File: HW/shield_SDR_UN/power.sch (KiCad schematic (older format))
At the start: 16 parts

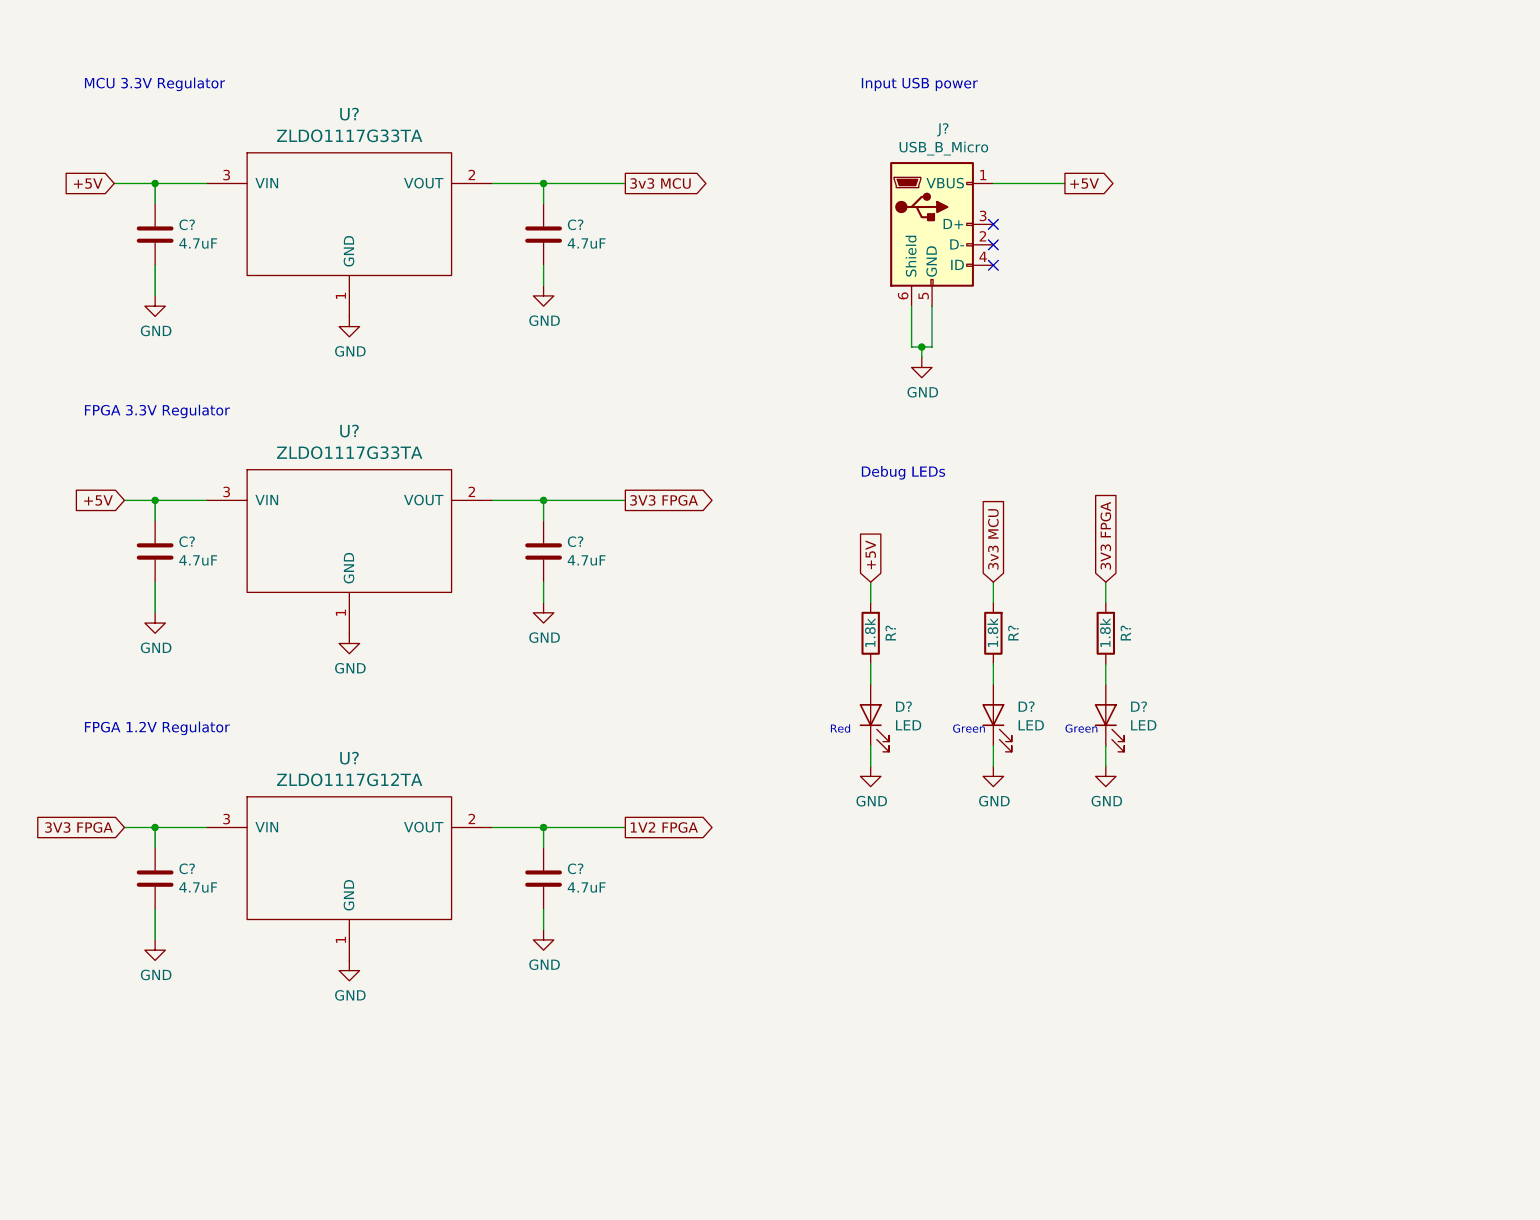
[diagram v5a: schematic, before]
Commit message: algunos footprint
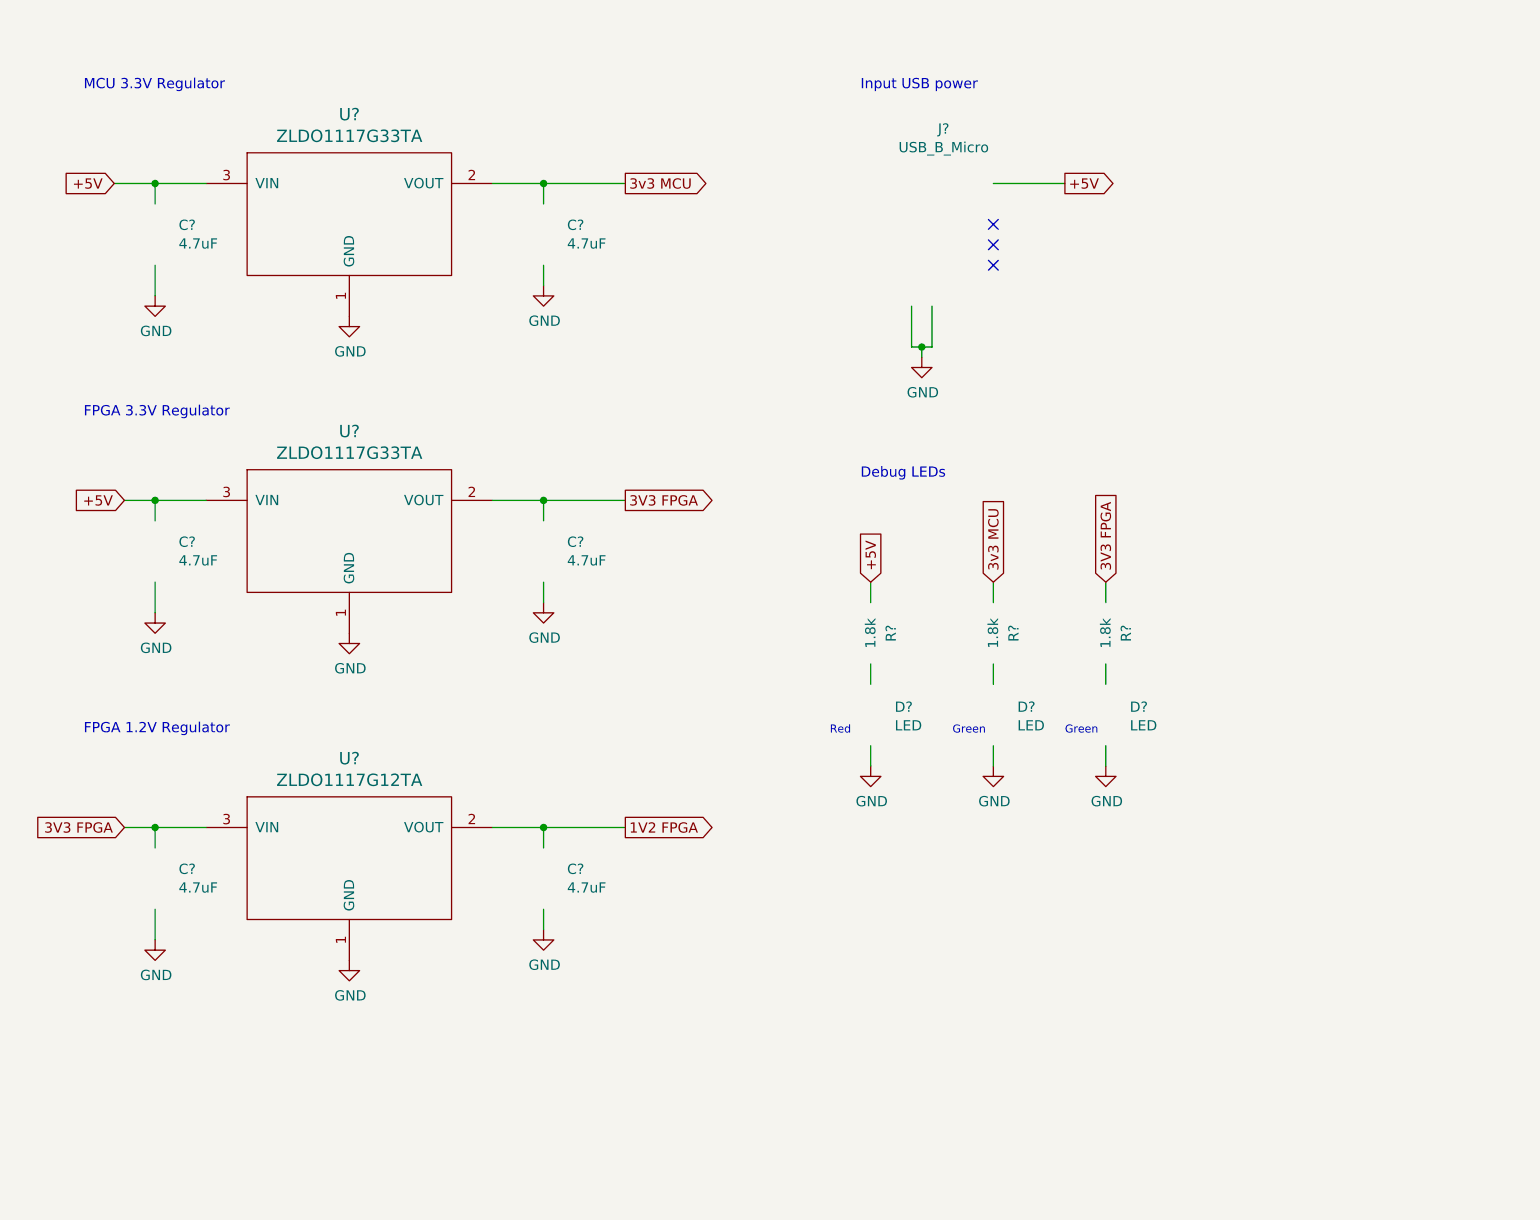
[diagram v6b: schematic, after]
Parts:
- C? (x6): footprint (none) -> Capacitor_SMD:C_0603_1608Metric_Pad1.05x0.95mm_HandSolder
- D? (x3): footprint (none) -> LED_SMD:LED_0805_2012Metric_Pad1.15x1.40mm_HandSolder
- J?: footprint (none) -> Connector_USB:USB_Micro-B_GCT_USB3076-30-A
- R? (x3): footprint (none) -> Resistor_SMD:R_0603_1608Metric_Pad1.05x0.95mm_HandSolder
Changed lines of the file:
@@
 $Comp
 L Device:C C?
-U 1 1 5CCD952E
+U 0 0 5CCD952E
 P 1550 3550
 F 0 "C?" H 1665 3596 50  0000 L CNN
 F 1 "4.7uF" H 1665 3505 50  0000 L CNN
-F 2 "" H 1588 3400 50  0001 C CNN
+F 2 "Capacitor_SMD:C_0603_1608Metric_Pad1.05x0.95mm_HandSolder" H 1588 3400 50  0001 C CNN
 F 3 "~" H 1550 3550 50  0001 C CNN
-	1    1550 3550
-	1    0    0    -1
-$EndComp
-$Comp
-L Device:C C?
-U 1 1 5CCDBE29
+	0    1550 3550
+	1    0    0    -1
+$EndComp
+$Comp
+L Device:C C?
+U 0 0 5CCDBE29
 P 3450 3550
 F 0 "C?" H 3565 3596 50  0000 L CNN
 F 1 "4.7uF" H 3565 3505 50  0000 L CNN
-F 2 "" H 3488 3400 50  0001 C CNN
+F 2 "Capacitor_SMD:C_0603_1608Metric_Pad1.05x0.95mm_HandSolder" H 3488 3400 50  0001 C CNN
 F 3 "~" H 3450 3550 50  0001 C CNN
-	1    3450 3550
+	0    3450 3550
 	1    0    0    -1
 $EndComp
@@
 	3450 3400 3450 3300
 $Comp
-L power:GND #PWR?
+L power:GND #PWR0180
 U 1 1 5CCE00C1
 P 3450 3800
-F 0 "#PWR?" H 3450 3550 50  0001 C CNN
+F 0 "#PWR0180" H 3450 3550 50  0001 C CNN
 F 1 "GND" H 3455 3627 50  0000 C CNN
 F 2 "" H 3450 3800 50  0001 C CNN
@@
 	3450 3700 3450 3800
 $Comp
-L power:GND #PWR?
+L power:GND #PWR0181
 U 1 1 5CCE4197
 P 1550 3850
-F 0 "#PWR?" H 1550 3600 50  0001 C CNN
+F 0 "#PWR0181" H 1550 3600 50  0001 C CNN
 F 1 "GND" H 1555 3677 50  0000 C CNN
 F 2 "" H 1550 3850 50  0001 C CNN
@@
 $Comp
 L Device:C C?
-U 1 1 5CCEBA00
+U 0 0 5CCEBA00
 P 1550 5150
 F 0 "C?" H 1665 5196 50  0000 L CNN
 F 1 "4.7uF" H 1665 5105 50  0000 L CNN
-F 2 "" H 1588 5000 50  0001 C CNN
+F 2 "Capacitor_SMD:C_0603_1608Metric_Pad1.05x0.95mm_HandSolder" H 1588 5000 50  0001 C CNN
 F 3 "~" H 1550 5150 50  0001 C CNN
-	1    1550 5150
+	0    1550 5150
 	1    0    0    -1
 $EndComp
@@
 	3450 5000 3450 4900
 $Comp
-L power:GND #PWR?
+L power:GND #PWR0182
 U 1 1 5CCEBA22
 P 3450 5400
-F 0 "#PWR?" H 3450 5150 50  0001 C CNN
+F 0 "#PWR0182" H 3450 5150 50  0001 C CNN
 F 1 "GND" H 3455 5227 50  0000 C CNN
 F 2 "" H 3450 5400 50  0001 C CNN
@@
 	1550 4900 1550 5000
 $Comp
-L power:GND #PWR?
+L power:GND #PWR0183
 U 1 1 5CCEBA40
 P 1550 5450
-F 0 "#PWR?" H 1550 5200 50  0001 C CNN
+F 0 "#PWR0183" H 1550 5200 50  0001 C CNN
 F 1 "GND" H 1555 5277 50  0000 C CNN
 F 2 "" H 1550 5450 50  0001 C CNN
@@
 $Comp
 L Device:C C?
-U 1 1 5CD3AA6A
+U 0 0 5CD3AA6A
 P 1550 2000
 F 0 "C?" H 1665 2046 50  0000 L CNN
 F 1 "4.7uF" H 1665 1955 50  0000 L CNN
-F 2 "" H 1588 1850 50  0001 C CNN
+F 2 "Capacitor_SMD:C_0603_1608Metric_Pad1.05x0.95mm_HandSolder" H 1588 1850 50  0001 C CNN
 F 3 "~" H 1550 2000 50  0001 C CNN
-	1    1550 2000
-	1    0    0    -1
-$EndComp
-$Comp
-L Device:C C?
-U 1 1 5CD3AA74
+	0    1550 2000
+	1    0    0    -1
+$EndComp
+$Comp
+L Device:C C?
+U 0 0 5CD3AA74
 P 3450 2000
 F 0 "C?" H 3565 2046 50  0000 L CNN
 F 1 "4.7uF" H 3565 1955 50  0000 L CNN
-F 2 "" H 3488 1850 50  0001 C CNN
+F 2 "Capacitor_SMD:C_0603_1608Metric_Pad1.05x0.95mm_HandSolder" H 3488 1850 50  0001 C CNN
 F 3 "~" H 3450 2000 50  0001 C CNN
-	1    3450 2000
+	0    3450 2000
 	1    0    0    -1
 $EndComp
@@
 	3450 1850 3450 1750
 $Comp
-L power:GND #PWR?
+L power:GND #PWR0184
 U 1 1 5CD3AA8C
 P 3450 2250
-F 0 "#PWR?" H 3450 2000 50  0001 C CNN
+F 0 "#PWR0184" H 3450 2000 50  0001 C CNN
 F 1 "GND" H 3455 2077 50  0000 C CNN
 F 2 "" H 3450 2250 50  0001 C CNN
@@
 	3450 2150 3450 2250
 $Comp
-L power:GND #PWR?
+L power:GND #PWR0185
 U 1 1 5CD3AAAA
 P 1550 2300
-F 0 "#PWR?" H 1550 2050 50  0001 C CNN
+F 0 "#PWR0185" H 1550 2050 50  0001 C CNN
 F 1 "GND" H 1555 2127 50  0000 C CNN
 F 2 "" H 1550 2300 50  0001 C CNN
@@
 $Comp
 L Connector:USB_B_Micro J?
-U 1 1 5D009192
+U 0 0 5D009192
 P 5350 1950
 F 0 "J?" H 5407 2417 50  0000 C CNN
 F 1 "USB_B_Micro" H 5407 2326 50  0000 C CNN
-F 2 "" H 5500 1900 50  0001 C CNN
+F 2 "Connector_USB:USB_Micro-B_GCT_USB3076-30-A" H 5500 1900 50  0001 C CNN
 F 3 "~" H 5500 1900 50  0001 C CNN
-	1    5350 1950
+	0    5350 1950
 	1    0    0    -1
 $EndComp
@@
 	5350 2550 5350 2350
 $Comp
-L power:GND #PWR?
+L power:GND #PWR0186
 U 1 1 5D010F02
 P 5300 2600
-F 0 "#PWR?" H 5300 2350 50  0001 C CNN
+F 0 "#PWR0186" H 5300 2350 50  0001 C CNN
 F 1 "GND" H 5305 2427 50  0000 C CNN
 F 2 "" H 5300 2600 50  0001 C CNN
@@
 $Comp
 L Device:C C?
-U 1 1 5CCEBA0A
+U 0 0 5CCEBA0A
 P 3450 5150
 F 0 "C?" H 3565 5196 50  0000 L CNN
 F 1 "4.7uF" H 3565 5105 50  0000 L CNN
-F 2 "" H 3488 5000 50  0001 C CNN
+F 2 "Capacitor_SMD:C_0603_1608Metric_Pad1.05x0.95mm_HandSolder" H 3488 5000 50  0001 C CNN
 F 3 "~" H 3450 5150 50  0001 C CNN
-	1    3450 5150
-	1    0    0    -1
-$EndComp
-$Comp
-L power:GND #PWR?
+	0    3450 5150
+	1    0    0    -1
+$EndComp
+$Comp
+L power:GND #PWR0187
 U 1 1 5CDC3540
 P 2500 3950
-F 0 "#PWR?" H 2500 3700 50  0001 C CNN
+F 0 "#PWR0187" H 2500 3700 50  0001 C CNN
 F 1 "GND" H 2505 3777 50  0000 C CNN
 F 2 "" H 2500 3950 50  0001 C CNN
@@
 $EndComp
 $Comp
-L power:GND #PWR?
+L power:GND #PWR0188
 U 1 1 5CDC3B98
 P 2500 2400
-F 0 "#PWR?" H 2500 2150 50  0001 C CNN
+F 0 "#PWR0188" H 2500 2150 50  0001 C CNN
 F 1 "GND" H 2505 2227 50  0000 C CNN
 F 2 "" H 2500 2400 50  0001 C CNN
@@
 $Comp
 L Device:R R?
-U 1 1 5CE70567
+U 0 0 5CE70567
 P 5050 3950
 AR Path="/5CC081D2/5CE70567" Ref="R?"  Part="1"
-AR Path="/5CC08321/5CE70567" Ref="R?"  Part="1"
+AR Path="/5CC08321/5CE70567" Ref="R?"  Part="0"
 F 0 "R?" V 4950 3950 50  0000 C CNN
 F 1 "1.8k" V 5050 3950 50  0000 C CNN
-F 2 "" V 4980 3950 50  0001 C CNN
+F 2 "Resistor_SMD:R_0603_1608Metric_Pad1.05x0.95mm_HandSolder" V 4980 3950 50  0001 C CNN
 F 3 "~" H 5050 3950 50  0001 C CNN
-	1    5050 3950
+	0    5050 3950
 	-1   0    0    1
 $EndComp
 $Comp
 L Device:LED D?
-U 1 1 5CE70571
+U 0 0 5CE70571
 P 5050 4350
 AR Path="/5CC081D2/5CE70571" Ref="D?"  Part="1"
-AR Path="/5CC08321/5CE70571" Ref="D?"  Part="1"
+AR Path="/5CC08321/5CE70571" Ref="D?"  Part="0"
 F 0 "D?" V 5089 4233 50  0000 R CNN
 F 1 "LED" V 4998 4233 50  0000 R CNN
-F 2 "" H 5050 4350 50  0001 C CNN
+F 2 "LED_SMD:LED_0805_2012Metric_Pad1.15x1.40mm_HandSolder" H 5050 4350 50  0001 C CNN
 F 3 "~" H 5050 4350 50  0001 C CNN
-	1    5050 4350
+	0    5050 4350
 	0    -1   -1   0
 $EndComp
@@
 	5050 3800 5050 3700
 $Comp
-L power:GND #PWR?
+L power:GND #PWR0189
 U 1 1 5CE7A2B5
 P 5050 4600
-F 0 "#PWR?" H 5050 4350 50  0001 C CNN
+F 0 "#PWR0189" H 5050 4350 50  0001 C CNN
 F 1 "GND" H 5055 4427 50  0000 C CNN
 F 2 "" H 5050 4600 50  0001 C CNN
@@
 $Comp
 L Device:R R?
-U 1 1 5CE85D9C
+U 0 0 5CE85D9C
 P 5650 3950
 AR Path="/5CC081D2/5CE85D9C" Ref="R?"  Part="1"
-AR Path="/5CC08321/5CE85D9C" Ref="R?"  Part="1"
+AR Path="/5CC08321/5CE85D9C" Ref="R?"  Part="0"
 F 0 "R?" V 5550 3950 50  0000 C CNN
 F 1 "1.8k" V 5650 3950 50  0000 C CNN
-F 2 "" V 5580 3950 50  0001 C CNN
+F 2 "Resistor_SMD:R_0603_1608Metric_Pad1.05x0.95mm_HandSolder" V 5580 3950 50  0001 C CNN
 F 3 "~" H 5650 3950 50  0001 C CNN
-	1    5650 3950
+	0    5650 3950
 	-1   0    0    1
 $EndComp
 $Comp
 L Device:LED D?
-U 1 1 5CE85DA6
+U 0 0 5CE85DA6
 P 5650 4350
 AR Path="/5CC081D2/5CE85DA6" Ref="D?"  Part="1"
-AR Path="/5CC08321/5CE85DA6" Ref="D?"  Part="1"
+AR Path="/5CC08321/5CE85DA6" Ref="D?"  Part="0"
 F 0 "D?" V 5689 4233 50  0000 R CNN
 F 1 "LED" V 5598 4233 50  0000 R CNN
-F 2 "" H 5650 4350 50  0001 C CNN
+F 2 "LED_SMD:LED_0805_2012Metric_Pad1.15x1.40mm_HandSolder" H 5650 4350 50  0001 C CNN
 F 3 "~" H 5650 4350 50  0001 C CNN
-	1    5650 4350
+	0    5650 4350
 	0    -1   -1   0
 $EndComp
@@
 	5650 3800 5650 3700
 $Comp
-L power:GND #PWR?
+L power:GND #PWR0190
 U 1 1 5CE85DB1
 P 5650 4600
-F 0 "#PWR?" H 5650 4350 50  0001 C CNN
+F 0 "#PWR0190" H 5650 4350 50  0001 C CNN
 F 1 "GND" H 5655 4427 50  0000 C CNN
 F 2 "" H 5650 4600 50  0001 C CNN
@@
 $Comp
 L Device:R R?
-U 1 1 5CE8EB5C
+U 0 0 5CE8EB5C
 P 6200 3950
 AR Path="/5CC081D2/5CE8EB5C" Ref="R?"  Part="1"
-AR Path="/5CC08321/5CE8EB5C" Ref="R?"  Part="1"
+AR Path="/5CC08321/5CE8EB5C" Ref="R?"  Part="0"
 F 0 "R?" V 6100 3950 50  0000 C CNN
 F 1 "1.8k" V 6200 3950 50  0000 C CNN
-F 2 "" V 6130 3950 50  0001 C CNN
+F 2 "Resistor_SMD:R_0603_1608Metric_Pad1.05x0.95mm_HandSolder" V 6130 3950 50  0001 C CNN
 F 3 "~" H 6200 3950 50  0001 C CNN
-	1    6200 3950
+	0    6200 3950
 	-1   0    0    1
 $EndComp
 $Comp
 L Device:LED D?
-U 1 1 5CE8EB66
+U 0 0 5CE8EB66
 P 6200 4350
 AR Path="/5CC081D2/5CE8EB66" Ref="D?"  Part="1"
-AR Path="/5CC08321/5CE8EB66" Ref="D?"  Part="1"
+AR Path="/5CC08321/5CE8EB66" Ref="D?"  Part="0"
 F 0 "D?" V 6239 4233 50  0000 R CNN
 F 1 "LED" V 6148 4233 50  0000 R CNN
-F 2 "" H 6200 4350 50  0001 C CNN
+F 2 "LED_SMD:LED_0805_2012Metric_Pad1.15x1.40mm_HandSolder" H 6200 4350 50  0001 C CNN
 F 3 "~" H 6200 4350 50  0001 C CNN
-	1    6200 4350
+	0    6200 4350
 	0    -1   -1   0
 $EndComp
@@
 	6200 3800 6200 3700
 $Comp
-L power:GND #PWR?
+L power:GND #PWR0191
 U 1 1 5CE8EB71
 P 6200 4600
-F 0 "#PWR?" H 6200 4350 50  0001 C CNN
+F 0 "#PWR0191" H 6200 4350 50  0001 C CNN
 F 1 "GND" H 6205 4427 50  0000 C CNN
 F 2 "" H 6200 4600 50  0001 C CNN
@@
 $EndComp
 $Comp
-L power:GND #PWR?
+L power:GND #PWR0192
 U 1 1 5CDC2FE1
 P 2500 5550
-F 0 "#PWR?" H 2500 5300 50  0001 C CNN
+F 0 "#PWR0192" H 2500 5300 50  0001 C CNN
 F 1 "GND" H 2505 5377 50  0000 C CNN
 F 2 "" H 2500 5550 50  0001 C CNN

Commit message: algunos footprint_v2
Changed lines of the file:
@@
 $Comp
 L Device:C C?
-U 0 0 5CCD952E
+U 1 1 5CCD952E
 P 1550 3550
 F 0 "C?" H 1665 3596 50  0000 L CNN
@@
 F 2 "Capacitor_SMD:C_0603_1608Metric_Pad1.05x0.95mm_HandSolder" H 1588 3400 50  0001 C CNN
 F 3 "~" H 1550 3550 50  0001 C CNN
-	0    1550 3550
-	1    0    0    -1
-$EndComp
-$Comp
-L Device:C C?
-U 0 0 5CCDBE29
+	1    1550 3550
+	1    0    0    -1
+$EndComp
+$Comp
+L Device:C C?
+U 1 1 5CCDBE29
 P 3450 3550
 F 0 "C?" H 3565 3596 50  0000 L CNN
@@
 F 2 "Capacitor_SMD:C_0603_1608Metric_Pad1.05x0.95mm_HandSolder" H 3488 3400 50  0001 C CNN
 F 3 "~" H 3450 3550 50  0001 C CNN
-	0    3450 3550
+	1    3450 3550
 	1    0    0    -1
 $EndComp
@@
 $Comp
 L Device:C C?
-U 0 0 5CCEBA00
+U 1 1 5CCEBA00
 P 1550 5150
 F 0 "C?" H 1665 5196 50  0000 L CNN
@@
 F 2 "Capacitor_SMD:C_0603_1608Metric_Pad1.05x0.95mm_HandSolder" H 1588 5000 50  0001 C CNN
 F 3 "~" H 1550 5150 50  0001 C CNN
-	0    1550 5150
+	1    1550 5150
 	1    0    0    -1
 $EndComp
@@
 $Comp
 L Device:C C?
-U 0 0 5CD3AA6A
+U 1 1 5CD3AA6A
 P 1550 2000
 F 0 "C?" H 1665 2046 50  0000 L CNN
@@
 F 2 "Capacitor_SMD:C_0603_1608Metric_Pad1.05x0.95mm_HandSolder" H 1588 1850 50  0001 C CNN
 F 3 "~" H 1550 2000 50  0001 C CNN
-	0    1550 2000
-	1    0    0    -1
-$EndComp
-$Comp
-L Device:C C?
-U 0 0 5CD3AA74
+	1    1550 2000
+	1    0    0    -1
+$EndComp
+$Comp
+L Device:C C?
+U 1 1 5CD3AA74
 P 3450 2000
 F 0 "C?" H 3565 2046 50  0000 L CNN
@@
 F 2 "Capacitor_SMD:C_0603_1608Metric_Pad1.05x0.95mm_HandSolder" H 3488 1850 50  0001 C CNN
 F 3 "~" H 3450 2000 50  0001 C CNN
-	0    3450 2000
+	1    3450 2000
 	1    0    0    -1
 $EndComp
@@
 $Comp
 L Connector:USB_B_Micro J?
-U 0 0 5D009192
+U 1 1 5D009192
 P 5350 1950
 F 0 "J?" H 5407 2417 50  0000 C CNN
@@
 F 2 "Connector_USB:USB_Micro-B_GCT_USB3076-30-A" H 5500 1900 50  0001 C CNN
 F 3 "~" H 5500 1900 50  0001 C CNN
-	0    5350 1950
+	1    5350 1950
 	1    0    0    -1
 $EndComp
@@
 $Comp
 L Device:C C?
-U 0 0 5CCEBA0A
+U 1 1 5CCEBA0A
 P 3450 5150
 F 0 "C?" H 3565 5196 50  0000 L CNN
@@
 F 2 "Capacitor_SMD:C_0603_1608Metric_Pad1.05x0.95mm_HandSolder" H 3488 5000 50  0001 C CNN
 F 3 "~" H 3450 5150 50  0001 C CNN
-	0    3450 5150
+	1    3450 5150
 	1    0    0    -1
 $EndComp
@@
 $Comp
 L Device:R R?
-U 0 0 5CE70567
+U 0 1 5CE70567
 P 5050 3950
 AR Path="/5CC081D2/5CE70567" Ref="R?"  Part="1"
@@
 $Comp
 L Device:LED D?
-U 0 0 5CE70571
+U 0 1 5CE70571
 P 5050 4350
 AR Path="/5CC081D2/5CE70571" Ref="D?"  Part="1"
@@
 $Comp
 L Device:R R?
-U 0 0 5CE85D9C
+U 0 1 5CE85D9C
 P 5650 3950
 AR Path="/5CC081D2/5CE85D9C" Ref="R?"  Part="1"
@@
 $Comp
 L Device:LED D?
-U 0 0 5CE85DA6
+U 0 1 5CE85DA6
 P 5650 4350
 AR Path="/5CC081D2/5CE85DA6" Ref="D?"  Part="1"
@@
 $Comp
 L Device:R R?
-U 0 0 5CE8EB5C
+U 0 1 5CE8EB5C
 P 6200 3950
 AR Path="/5CC081D2/5CE8EB5C" Ref="R?"  Part="1"
@@
 $Comp
 L Device:LED D?
-U 0 0 5CE8EB66
+U 0 1 5CE8EB66
 P 6200 4350
 AR Path="/5CC081D2/5CE8EB66" Ref="D?"  Part="1"

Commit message: RF-Frontend balun
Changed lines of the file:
@@
 $Comp
 L Device:R R?
-U 0 1 5CE70567
+U 1 1 5CE70567
 P 5050 3950
 AR Path="/5CC081D2/5CE70567" Ref="R?"  Part="1"
@@
 F 2 "Resistor_SMD:R_0603_1608Metric_Pad1.05x0.95mm_HandSolder" V 4980 3950 50  0001 C CNN
 F 3 "~" H 5050 3950 50  0001 C CNN
-	0    5050 3950
+	1    5050 3950
 	-1   0    0    1
 $EndComp
 $Comp
 L Device:LED D?
-U 0 1 5CE70571
+U 1 1 5CE70571
 P 5050 4350
 AR Path="/5CC081D2/5CE70571" Ref="D?"  Part="1"
@@
 F 2 "LED_SMD:LED_0805_2012Metric_Pad1.15x1.40mm_HandSolder" H 5050 4350 50  0001 C CNN
 F 3 "~" H 5050 4350 50  0001 C CNN
-	0    5050 4350
+	1    5050 4350
 	0    -1   -1   0
 $EndComp
@@
 $Comp
 L Device:R R?
-U 0 1 5CE85D9C
+U 1 1 5CE85D9C
 P 5650 3950
 AR Path="/5CC081D2/5CE85D9C" Ref="R?"  Part="1"
@@
 F 2 "Resistor_SMD:R_0603_1608Metric_Pad1.05x0.95mm_HandSolder" V 5580 3950 50  0001 C CNN
 F 3 "~" H 5650 3950 50  0001 C CNN
-	0    5650 3950
+	1    5650 3950
 	-1   0    0    1
 $EndComp
 $Comp
 L Device:LED D?
-U 0 1 5CE85DA6
+U 1 1 5CE85DA6
 P 5650 4350
 AR Path="/5CC081D2/5CE85DA6" Ref="D?"  Part="1"
@@
 F 2 "LED_SMD:LED_0805_2012Metric_Pad1.15x1.40mm_HandSolder" H 5650 4350 50  0001 C CNN
 F 3 "~" H 5650 4350 50  0001 C CNN
-	0    5650 4350
+	1    5650 4350
 	0    -1   -1   0
 $EndComp
@@
 $Comp
 L Device:R R?
-U 0 1 5CE8EB5C
+U 1 1 5CE8EB5C
 P 6200 3950
 AR Path="/5CC081D2/5CE8EB5C" Ref="R?"  Part="1"
@@
 F 2 "Resistor_SMD:R_0603_1608Metric_Pad1.05x0.95mm_HandSolder" V 6130 3950 50  0001 C CNN
 F 3 "~" H 6200 3950 50  0001 C CNN
-	0    6200 3950
+	1    6200 3950
 	-1   0    0    1
 $EndComp
 $Comp
 L Device:LED D?
-U 0 1 5CE8EB66
+U 1 1 5CE8EB66
 P 6200 4350
 AR Path="/5CC081D2/5CE8EB66" Ref="D?"  Part="1"
@@
 F 2 "LED_SMD:LED_0805_2012Metric_Pad1.15x1.40mm_HandSolder" H 6200 4350 50  0001 C CNN
 F 3 "~" H 6200 4350 50  0001 C CNN
-	0    6200 4350
+	1    6200 4350
 	0    -1   -1   0
 $EndComp
